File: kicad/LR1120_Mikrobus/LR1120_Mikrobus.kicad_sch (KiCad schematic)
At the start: 90 parts, among them Q1 NX2016SA-32M-EXS00A-CS06465, Q2 NT2016SA-32M-END4263A, Q3 NX3215SA, U1 LR1120, U2 SKY13588-460LF, U5 LIS2DE12, U7 M24128-BFMH6TG, U8 BGA524N6E6327XTSA1

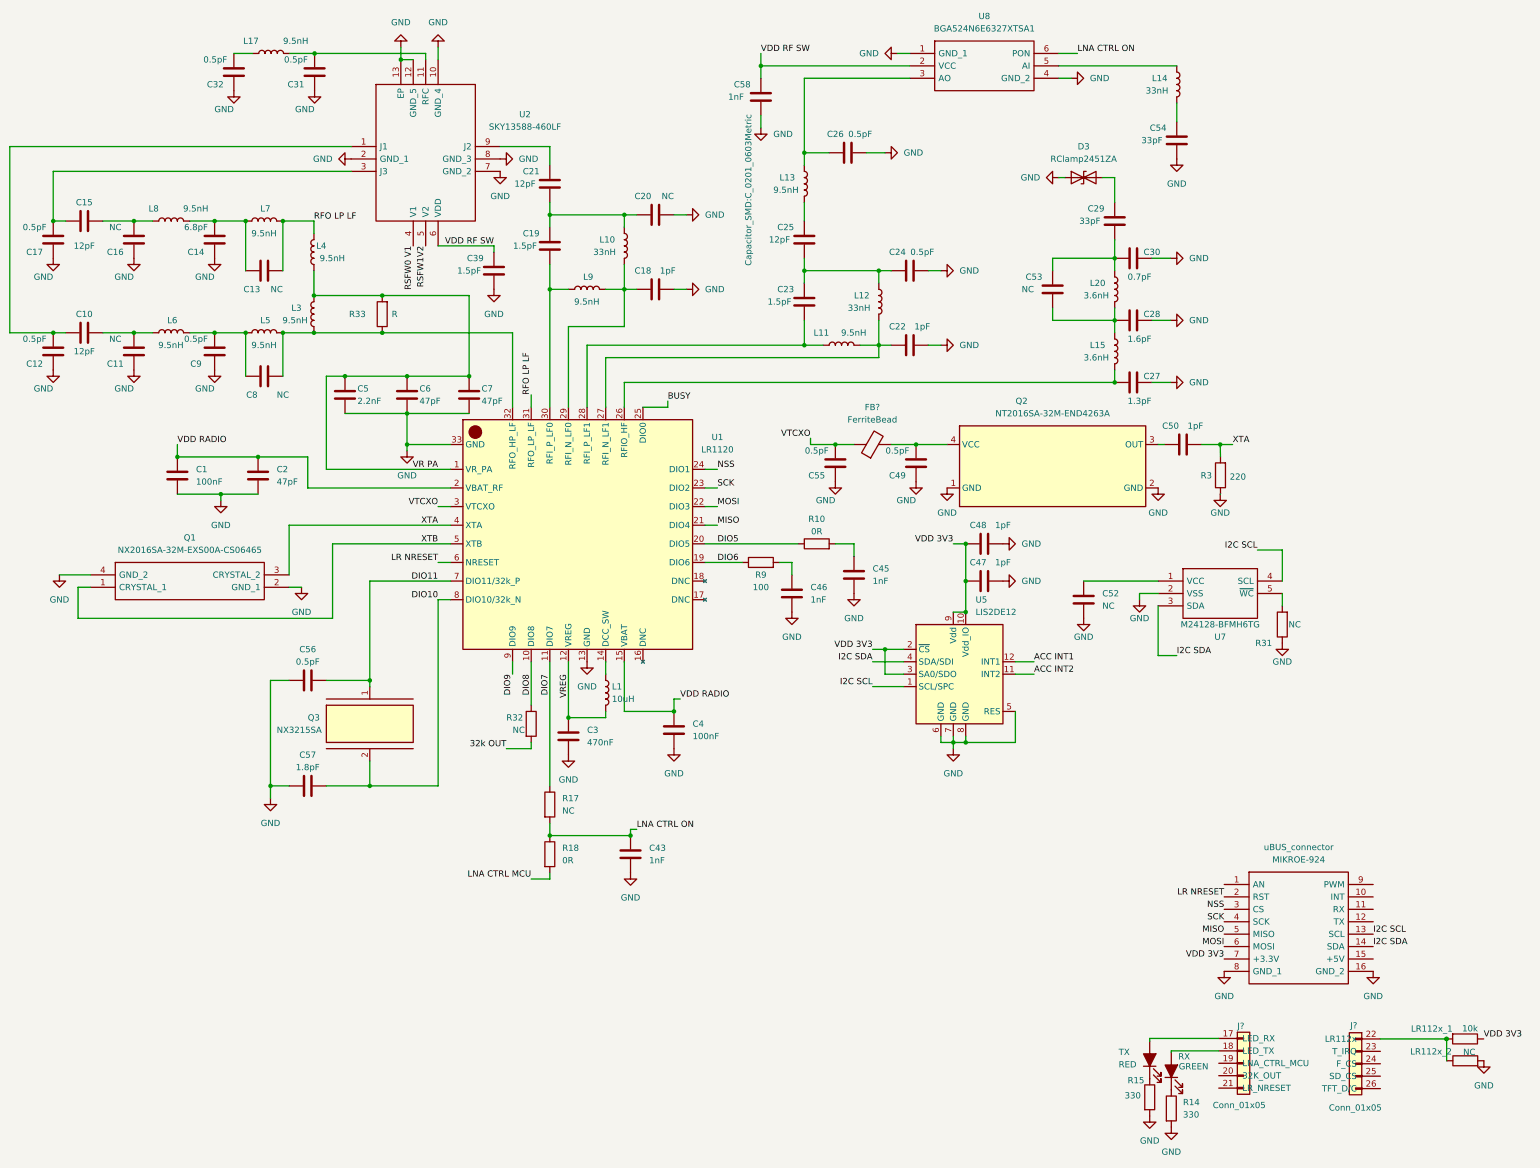
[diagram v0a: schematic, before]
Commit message: Commit finish display
The connector of mimkrobus were changed with correct names, without changing the standard value like was in the last commit.

LNA CTRL MCU added to mikrobus

32k OUT added to mikrobus

DISP_RESET, T_IRQ, F_CS and TFT_D/C doesn't exist as label in the sheet, they are display labels. This labels were
created and add to mikrobus.
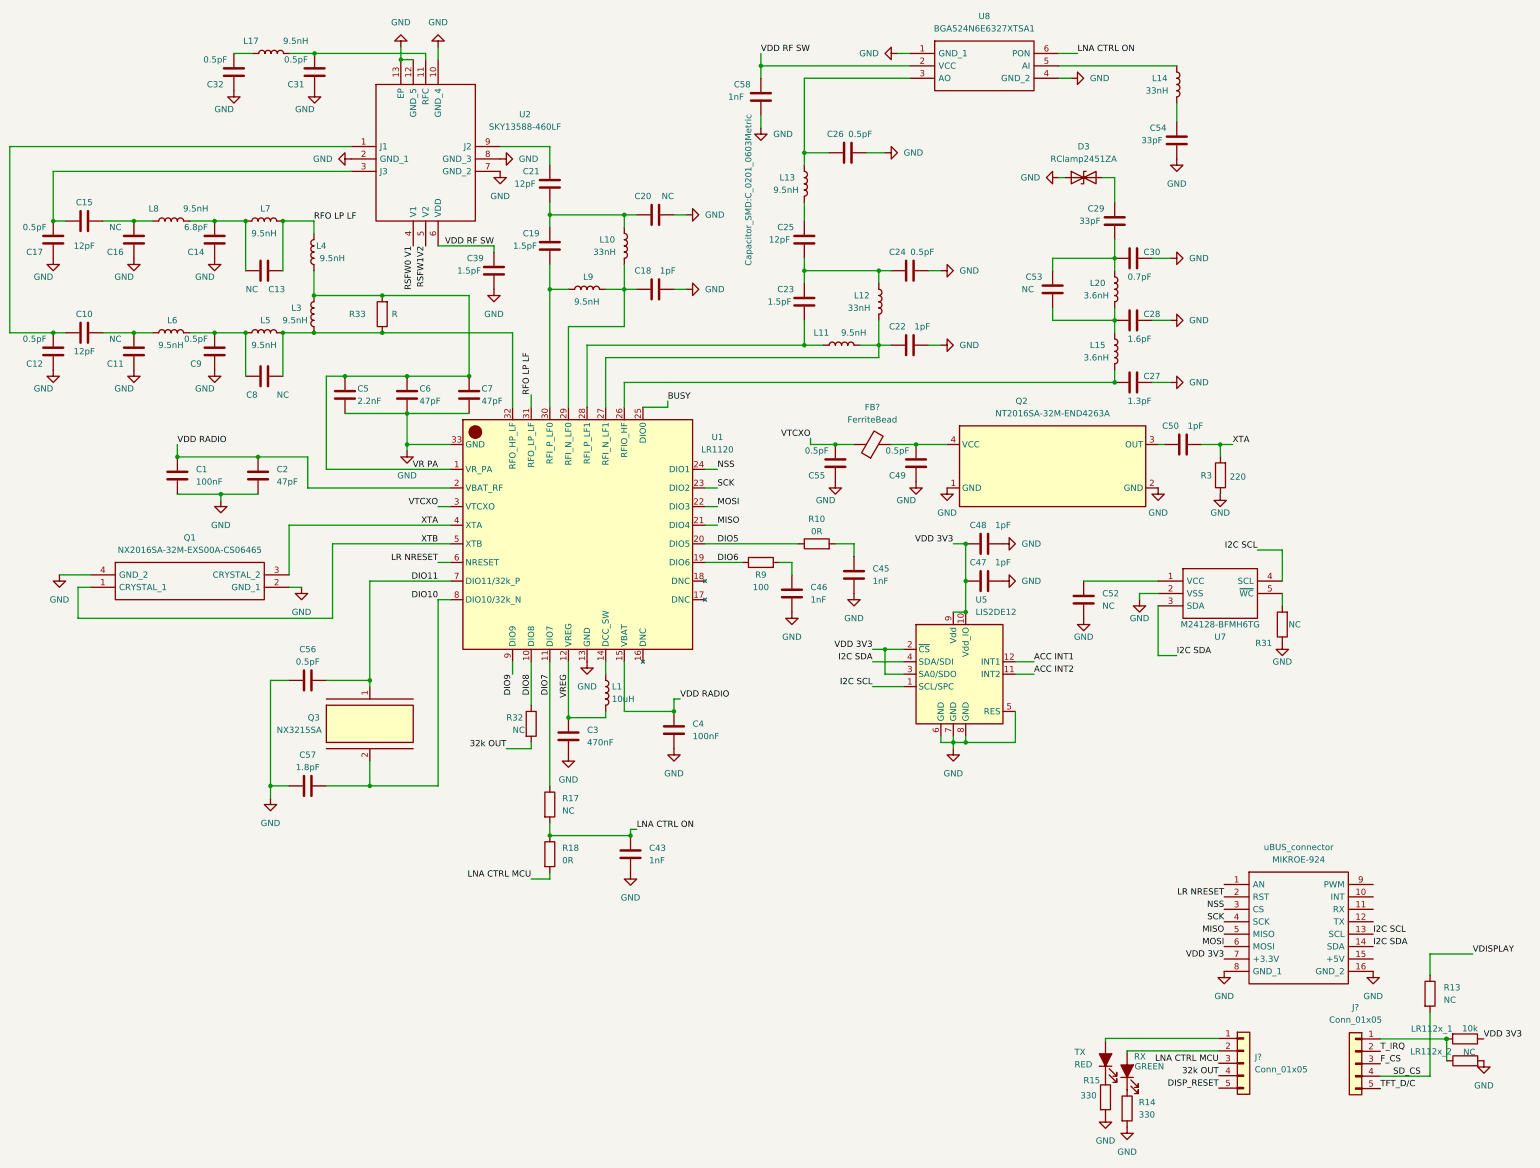
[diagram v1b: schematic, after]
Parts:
- removed J? (x2): Conn_01x05, symbol Connector_Generic:Conn_01x05
- added J? (x2): Conn_01x05, symbol Connector_Generic:Conn_01x05
- added R13: NC, symbol Device:R
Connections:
- net 32k OUT: now also J?.4 (Pin_4)
- net LNA CTRL MCU: now also J?.3 (Pin_3)
- net RFO LP LF: now also C13.2; no longer C13.1
- net at RX.2 (A): now also J?.2 (Pin_2)
- net at TX.2 (A): now also J?.1 (Pin_1)
- net at LR112x_1.2, LR112x_2.1: now also J?.1 (Pin_1)
- net at C14.1, L7.1, L8.2: now also C13.1; no longer C13.2
- new net DISP_RESET: J?.5 (Pin_5)
- new net F_CS: J?.3 (Pin_3)
- new net SD_CS: J?.4 (Pin_4), R13.2
- new net TFT_D/C: J?.5 (Pin_5)
- new net T_IRQ: J?.2 (Pin_2)
- new net VDISPLAY: R13.1
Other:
- moved on the sheet: C13, R14, R15, RX, TX

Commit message: R13 footprint added
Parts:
- R13: footprint (none) -> Resistor_SMD:R_0201_0603Metric
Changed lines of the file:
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@@
       (effects (font (size 1.27 1.27)) (justify left))
     )
-    (property "Footprint" "" (id 2) (at 307.848 212.6996 90)
+    (property "Footprint" "Resistor_SMD:R_0201_0603Metric" (id 2) (at 307.848 212.6996 90)
       (effects (font (size 1.27 1.27)) hide)
     )
@@
     )
     (path "/9a502a54-b95a-4145-b7b6-90757806098f"
-      (reference "R13") (unit 1) (value "NC") (footprint "")
+      (reference "R13") (unit 1) (value "NC") (footprint "Resistor_SMD:R_0201_0603Metric")
     )
     (path "/9c0cad7c-1634-4e6a-beb7-e9016b86f636"

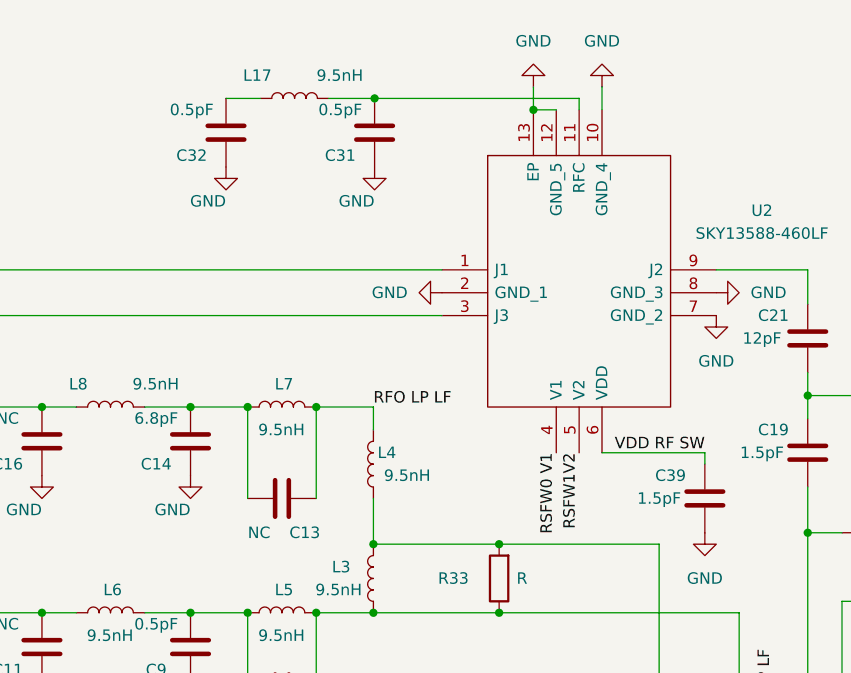
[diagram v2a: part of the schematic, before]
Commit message: Capacitor values changed
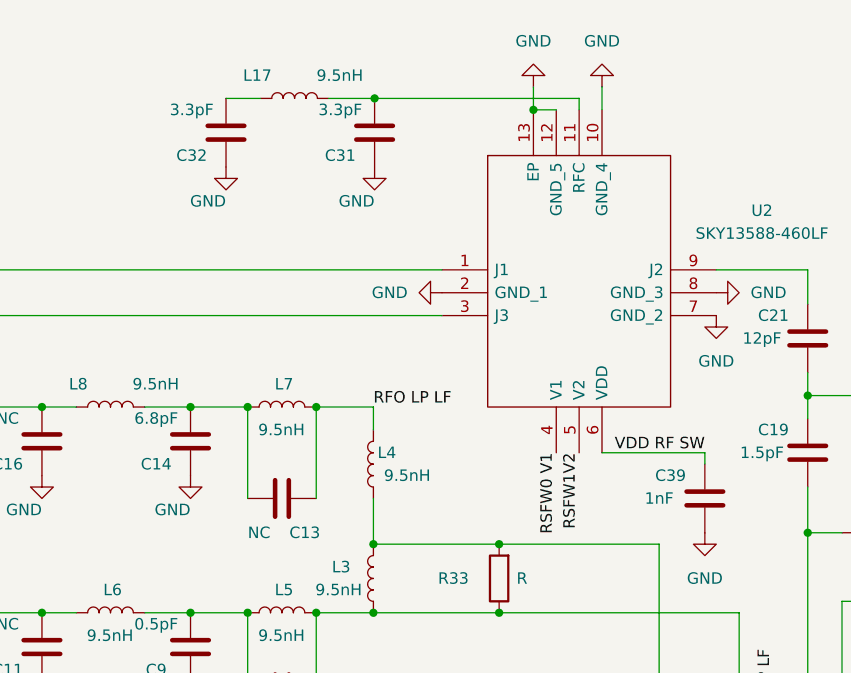
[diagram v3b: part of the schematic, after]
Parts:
- C31, C32: value 0.5pF -> 3.3pF
- C39: value 1.5pF -> 1nF; footprint Capacitor_SMD:C_01005_0402Metric -> Capacitor_SMD:C_0201_0603Metric
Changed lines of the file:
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@@
     (in_bom yes) (on_board yes)
     (property "Reference" "C31" (id 0) (at 77.6033 26.67 0))
-    (property "Value" "0.5pF" (id 1) (at 77.6033 21.59 0))
+    (property "Value" "3.3pF" (id 1) (at 77.6033 21.59 0))
     (property "Footprint" "Capacitor_SMD:C_01005_0402Metric" (id 2) (at 82.3785 27.94 0)
       (effects (font (size 1.27 1.27)) hide)
@@
     (in_bom yes) (on_board yes)
     (property "Reference" "C39" (id 0) (at 114.3 62.23 0))
-    (property "Value" "1.5pF" (id 1) (at 113.03 64.77 0))
-    (property "Footprint" "Capacitor_SMD:C_01005_0402Metric" (id 2) (at 117.1448 60.96 0)
+    (property "Value" "1nF" (id 1) (at 113.03 64.77 0))
+    (property "Footprint" "Capacitor_SMD:C_0201_0603Metric" (id 2) (at 117.1448 60.96 0)
       (effects (font (size 1.27 1.27)) hide)
     )
@@
     (in_bom yes) (on_board yes)
     (property "Reference" "C32" (id 0) (at 61.0933 26.67 0))
-    (property "Value" "0.5pF" (id 1) (at 61.0933 21.59 0))
+    (property "Value" "3.3pF" (id 1) (at 61.0933 21.59 0))
     (property "Footprint" "Capacitor_SMD:C_01005_0402Metric" (id 2) (at 65.8685 27.94 0)
       (effects (font (size 1.27 1.27)) hide)
@@
     )
     (path "/012309f5-a6a0-4583-8e38-6c6c5d95713d"
-      (reference "C31") (unit 1) (value "0.5pF") (footprint "Capacitor_SMD:C_01005_0402Metric")
+      (reference "C31") (unit 1) (value "3.3pF") (footprint "Capacitor_SMD:C_01005_0402Metric")
     )
     (path "/71a7a4e6-1282-4524-8e85-355c6dfffdef"
-      (reference "C32") (unit 1) (value "0.5pF") (footprint "Capacitor_SMD:C_01005_0402Metric")
+      (reference "C32") (unit 1) (value "3.3pF") (footprint "Capacitor_SMD:C_01005_0402Metric")
     )
     (path "/11b52c0d-1501-4ac2-a2b2-6111914506ee"
-      (reference "C39") (unit 1) (value "1.5pF") (footprint "Capacitor_SMD:C_01005_0402Metric")
+      (reference "C39") (unit 1) (value "1nF") (footprint "Capacitor_SMD:C_0201_0603Metric")
     )
     (path "/5dbc0070-a676-4f5d-8148-b0b3d222c548"
